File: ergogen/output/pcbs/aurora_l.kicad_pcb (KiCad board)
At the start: 2 copper layers, 145.1 x 101.4 mm, 90 parts

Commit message: Organize pins and clean up led footprint
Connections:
- net P113 renamed P11
- REF** pad 1: VCC -> P010 (x28)
- REF** pad 2: P010 -> VCC (x28)
- REF** pad 3: GND -> P009 (x28)
- REF** pad 4: P009 -> GND (x28)
- S25 pad 2: P011 -> P01
- S26 pad 2: P100 -> P02
- S27 pad 2: P022 -> P03
- S28 pad 2: P017 -> P05

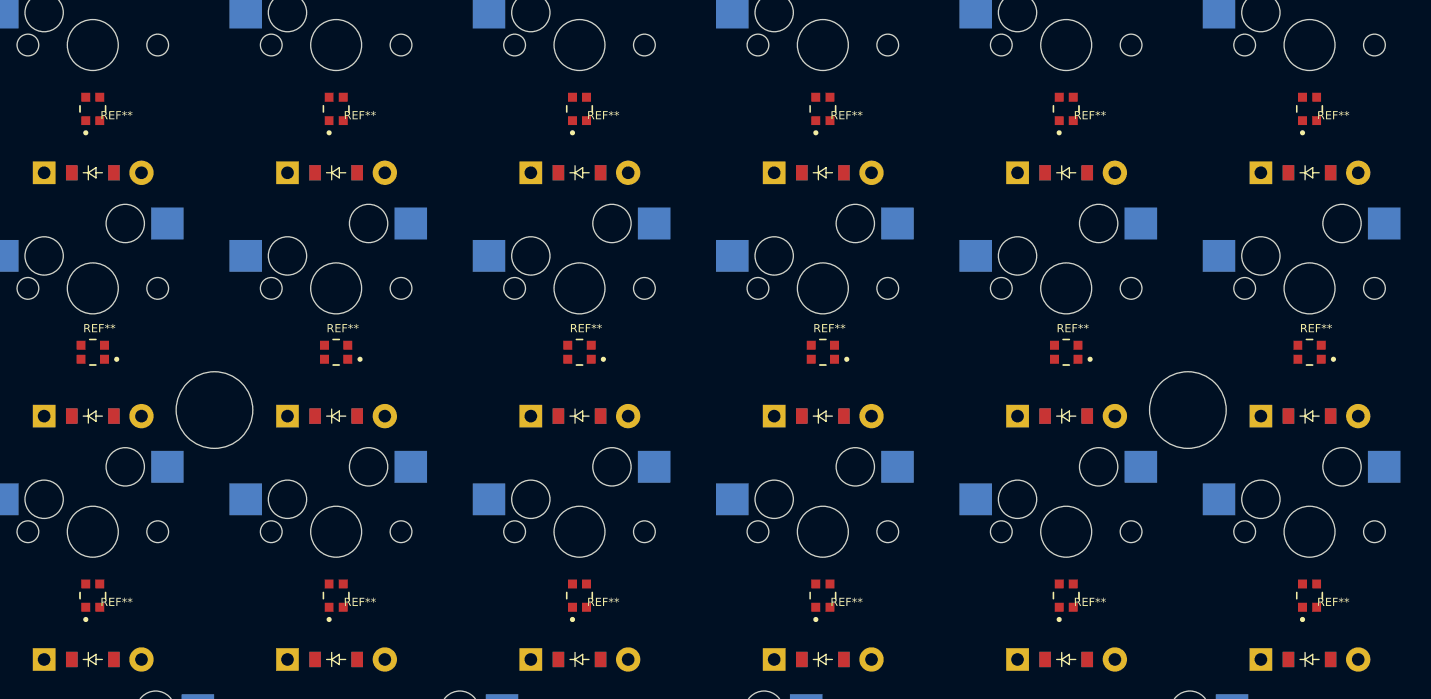
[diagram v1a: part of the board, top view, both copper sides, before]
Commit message: Simplify LED rotations
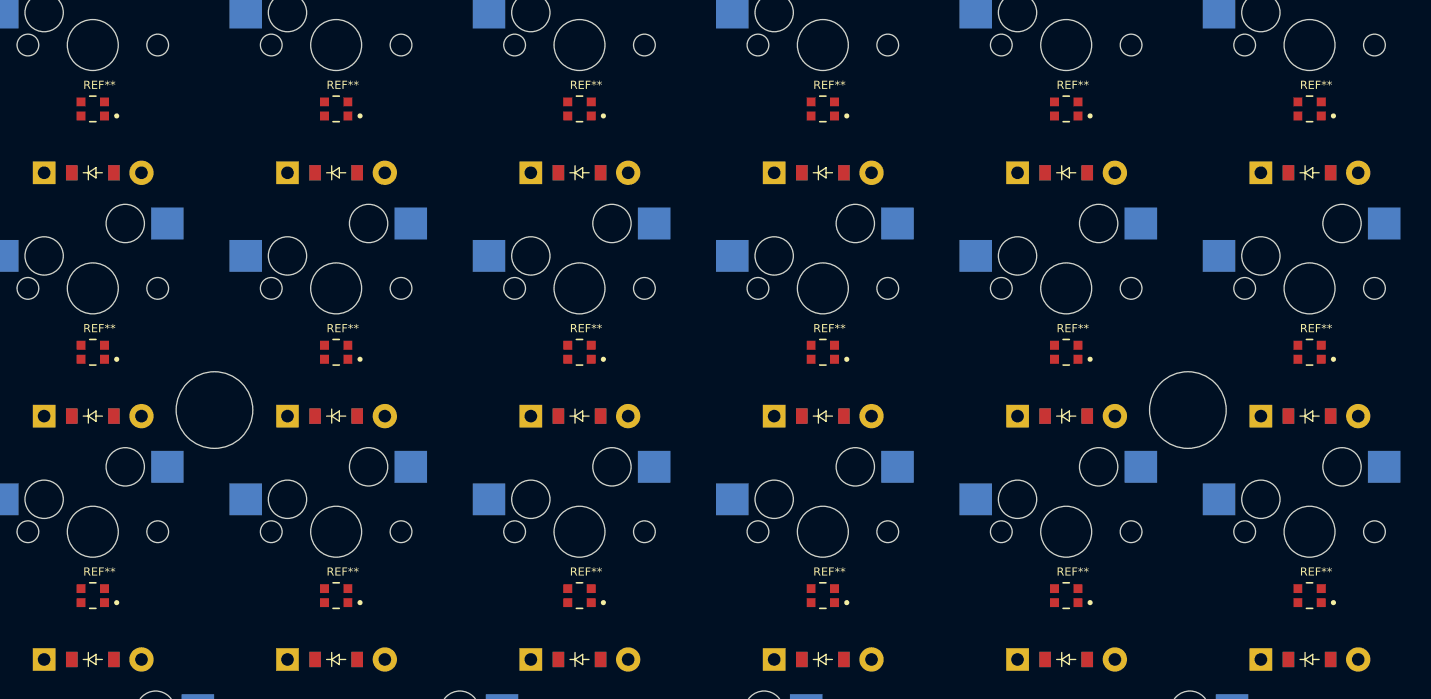
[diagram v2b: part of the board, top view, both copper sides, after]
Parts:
- turned REF** to 0 degrees (x12)
